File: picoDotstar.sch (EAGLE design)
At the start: 17 parts

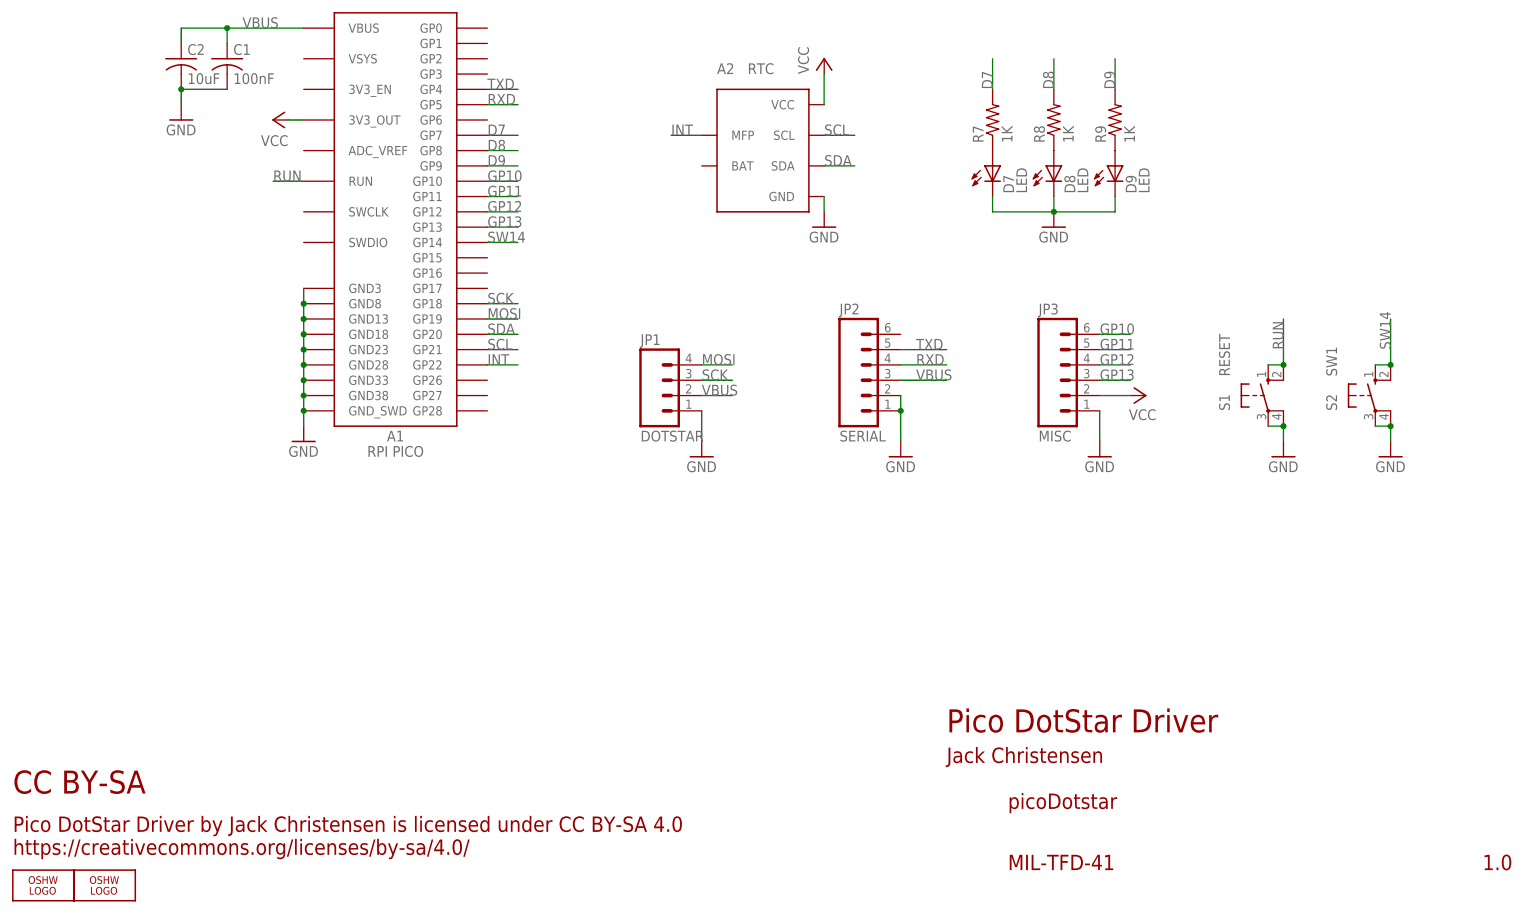
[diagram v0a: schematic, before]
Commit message: Move RTC from I2C0 to I2C1.
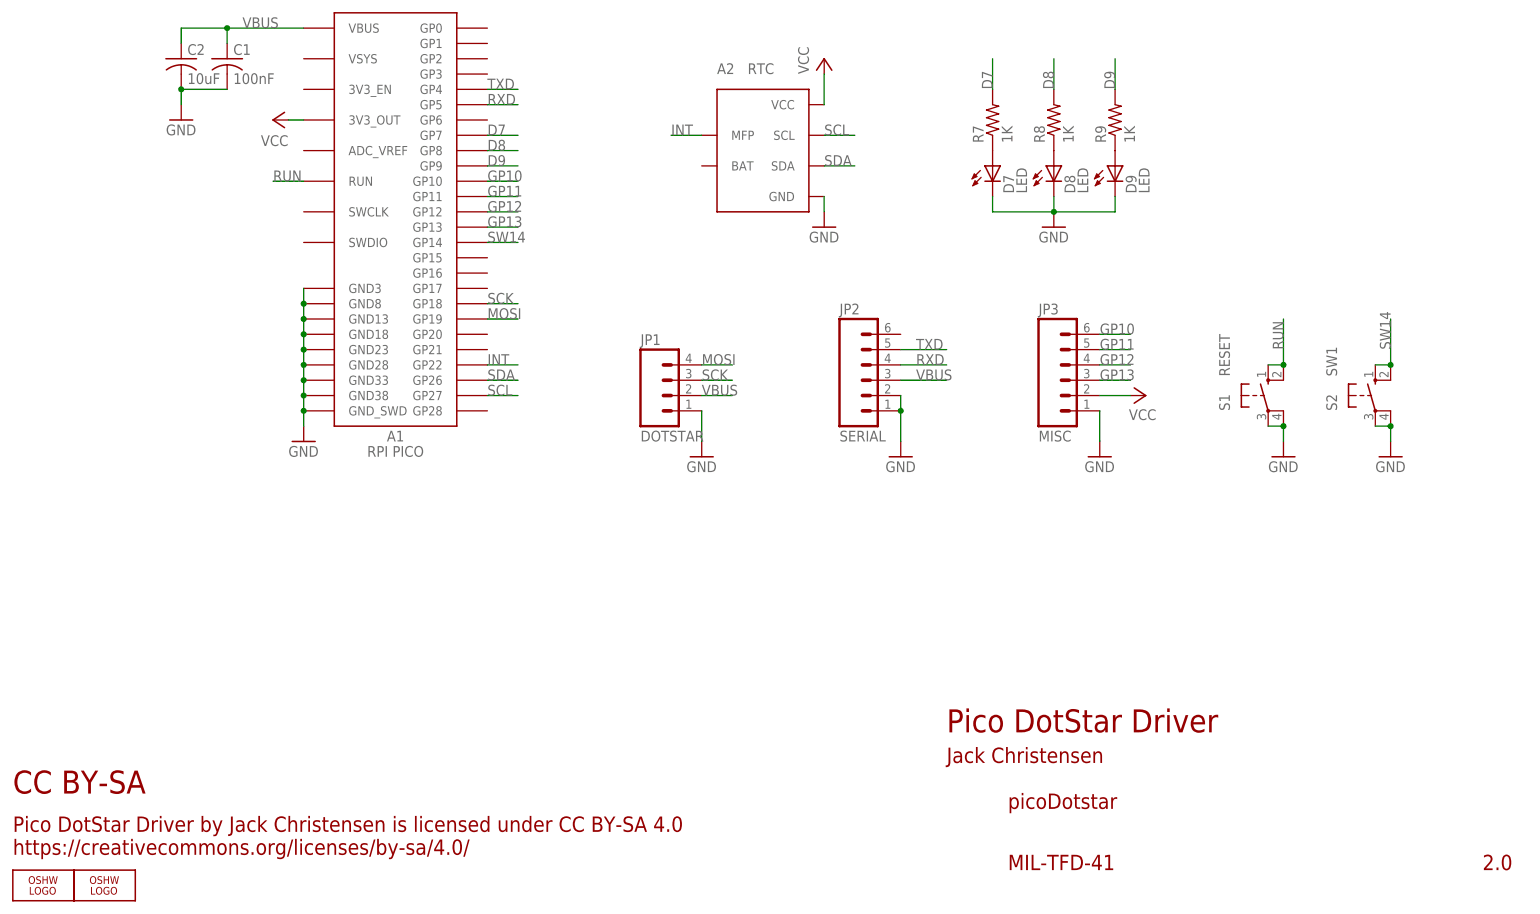
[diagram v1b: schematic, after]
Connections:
- net SCL: now also A1.GP27; no longer A1.GP21
- net SDA: now also A1.GP26; no longer A1.GP20
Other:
- note added: "2.0"
- note removed: "1.0"
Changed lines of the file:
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@@
 <grid distance="0.1" unitdist="inch" unit="inch" style="lines" multiple="1" display="no" altdistance="0.01" altunitdist="inch" altunit="inch"/>
 <layers>
-<layer number="1" name="Top" color="4" fill="1" visible="no" active="no"/>
-<layer number="16" name="Bottom" color="1" fill="1" visible="no" active="no"/>
-<layer number="17" name="Pads" color="2" fill="1" visible="no" active="no"/>
-<layer number="18" name="Vias" color="2" fill="1" visible="no" active="no"/>
-<layer number="19" name="Unrouted" color="6" fill="1" visible="no" active="no"/>
-<layer number="20" name="Dimension" color="15" fill="1" visible="no" active="no"/>
-<layer number="21" name="tPlace" color="7" fill="1" visible="no" active="no"/>
-<layer number="22" name="bPlace" color="7" fill="1" visible="no" active="no"/>
-<layer number="23" name="tOrigins" color="15" fill="1" visible="no" active="no"/>
-<layer number="24" name="bOrigins" color="15" fill="1" visible="no" active="no"/>
-<layer number="25" name="tNames" color="7" fill="1" visible="no" active="no"/>
-<layer number="26" name="bNames" color="7" fill="1" visible="no" active="no"/>
-<layer number="27" name="tValues" color="7" fill="1" visible="no" active="no"/>
-<layer number="28" name="bValues" color="7" fill="1" visible="no" active="no"/>
+<layer number="1" name="Top" color="4" fill="1" visible="yes" active="no"/>
+<layer number="16" name="Bottom" color="1" fill="1" visible="yes" active="no"/>
+<layer number="17" name="Pads" color="2" fill="1" visible="yes" active="no"/>
+<layer number="18" name="Vias" color="2" fill="1" visible="yes" active="no"/>
+<layer number="19" name="Unrouted" color="6" fill="1" visible="yes" active="no"/>
+<layer number="20" name="Dimension" color="24" fill="1" visible="yes" active="no"/>
+<layer number="21" name="tPlace" color="7" fill="1" visible="yes" active="no"/>
+<layer number="22" name="bPlace" color="7" fill="1" visible="yes" active="no"/>
+<layer number="23" name="tOrigins" color="15" fill="1" visible="yes" active="no"/>
+<layer number="24" name="bOrigins" color="15" fill="1" visible="yes" active="no"/>
+<layer number="25" name="tNames" color="7" fill="1" visible="yes" active="no"/>
+<layer number="26" name="bNames" color="7" fill="1" visible="yes" active="no"/>
+<layer number="27" name="tValues" color="7" fill="1" visible="yes" active="no"/>
+<layer number="28" name="bValues" color="7" fill="1" visible="yes" active="no"/>
 <layer number="29" name="tStop" color="7" fill="3" visible="no" active="no"/>
 <layer number="30" name="bStop" color="7" fill="6" visible="no" active="no"/>
@@
 <layer number="35" name="tGlue" color="7" fill="4" visible="no" active="no"/>
 <layer number="36" name="bGlue" color="7" fill="5" visible="no" active="no"/>
-<layer number="37" name="tTest" color="7" fill="1" visible="no" active="no"/>
-<layer number="38" name="bTest" color="7" fill="1" visible="no" active="no"/>
+<layer number="37" name="tTest" color="7" fill="1" visible="yes" active="no"/>
+<layer number="38" name="bTest" color="7" fill="1" visible="yes" active="no"/>
 <layer number="39" name="tKeepout" color="4" fill="11" visible="no" active="no"/>
 <layer number="40" name="bKeepout" color="1" fill="11" visible="no" active="no"/>
@@
 <layer number="44" name="Drills" color="7" fill="1" visible="no" active="no"/>
 <layer number="45" name="Holes" color="7" fill="1" visible="no" active="no"/>
-<layer number="46" name="Milling" color="3" fill="1" visible="no" active="no"/>
-<layer number="47" name="Measures" color="7" fill="1" visible="no" active="no"/>
-<layer number="48" name="Document" color="7" fill="1" visible="no" active="no"/>
-<layer number="49" name="Reference" color="7" fill="1" visible="no" active="no"/>
-<layer number="50" name="dxf" color="7" fill="1" visible="no" active="no"/>
-<layer number="51" name="tDocu" color="7" fill="1" visible="no" active="no"/>
-<layer number="52" name="bDocu" color="7" fill="1" visible="no" active="no"/>
-<layer number="53" name="tGND_GNDA" color="7" fill="9" visible="no" active="no"/>
-<layer number="54" name="bGND_GNDA" color="1" fill="9" visible="no" active="no"/>
-<layer number="56" name="wert" color="7" fill="1" visible="no" active="no"/>
-<layer number="57" name="tCAD" color="7" fill="1" visible="no" active="no"/>
-<layer number="59" name="tCarbon" color="7" fill="1" visible="no" active="no"/>
-<layer number="60" name="bCarbon" color="7" fill="1" visible="no" active="no"/>
+<layer number="46" name="Milling" color="3" fill="1" visible="yes" active="no"/>
+<layer number="47" name="Measures" color="7" fill="1" visible="yes" active="no"/>
+<layer number="48" name="Document" color="7" fill="1" visible="yes" active="no"/>
+<layer number="49" name="Reference" color="7" fill="1" visible="yes" active="no"/>
+<layer number="50" name="dxf" color="7" fill="1" visible="yes" active="no"/>
+<layer number="51" name="tDocu" color="7" fill="1" visible="yes" active="no"/>
+<layer number="52" name="bDocu" color="7" fill="1" visible="yes" active="no"/>
+<layer number="53" name="tGND_GNDA" color="7" fill="9" visible="yes" active="no"/>
+<layer number="54" name="bGND_GNDA" color="1" fill="9" visible="yes" active="no"/>
+<layer number="56" name="wert" color="7" fill="1" visible="yes" active="no"/>
+<layer number="57" name="tCAD" color="7" fill="1" visible="yes" active="no"/>
+<layer number="59" name="tCarbon" color="7" fill="1" visible="yes" active="no"/>
+<layer number="60" name="bCarbon" color="7" fill="1" visible="yes" active="no"/>
 <layer number="88" name="SimResults" color="9" fill="1" visible="yes" active="yes"/>
 <layer number="89" name="SimProbes" color="9" fill="1" visible="yes" active="yes"/>
@@
 <text x="175.26" y="25.4" size="2.54" layer="94" ratio="10">Jack Christensen</text>
 <text x="185.42" y="17.78" size="2.54" layer="94" ratio="10">picoDotstar</text>
-<text x="264.16" y="7.62" size="2.54" layer="94" ratio="10">1.0</text>
+<text x="264.16" y="7.62" size="2.54" layer="94" ratio="10">2.0</text>
 <text x="20.32" y="20.32" size="3.81" layer="94" ratio="12">CC BY-SA</text>
 <text x="20.32" y="10.16" size="2.54" layer="94" ratio="10">Pico DotStar Driver by Jack Christensen is licensed under CC BY-SA 4.0
@@
 </segment>
 <segment>
-<pinref part="A1" gate="G$1" pin="GP21"/>
-<wire x1="99.06" y1="93.98" x2="104.14" y2="93.98" width="0.1524" layer="91"/>
-<label x="99.06" y="93.98" size="1.778" layer="95"/>
+<pinref part="A1" gate="G$1" pin="GP27"/>
+<wire x1="99.06" y1="86.36" x2="104.14" y2="86.36" width="0.1524" layer="91"/>
+<label x="99.06" y="86.36" size="1.778" layer="95"/>
 </segment>
 </net>
@@
 </segment>
 <segment>
-<pinref part="A1" gate="G$1" pin="GP20"/>
-<wire x1="99.06" y1="96.52" x2="104.14" y2="96.52" width="0.1524" layer="91"/>
-<label x="99.06" y="96.52" size="1.778" layer="95"/>
-</segment>
-</net>
+<pinref part="A1" gate="G$1" pin="GP26"/>
+<wire x1="99.06" y1="88.9" x2="104.14" y2="88.9" width="0.1524" layer="91"/>
+<label x="99.06" y="88.9" size="1.778" layer="95"/>
+</segment>
+</net>
